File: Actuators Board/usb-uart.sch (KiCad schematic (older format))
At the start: 15 parts

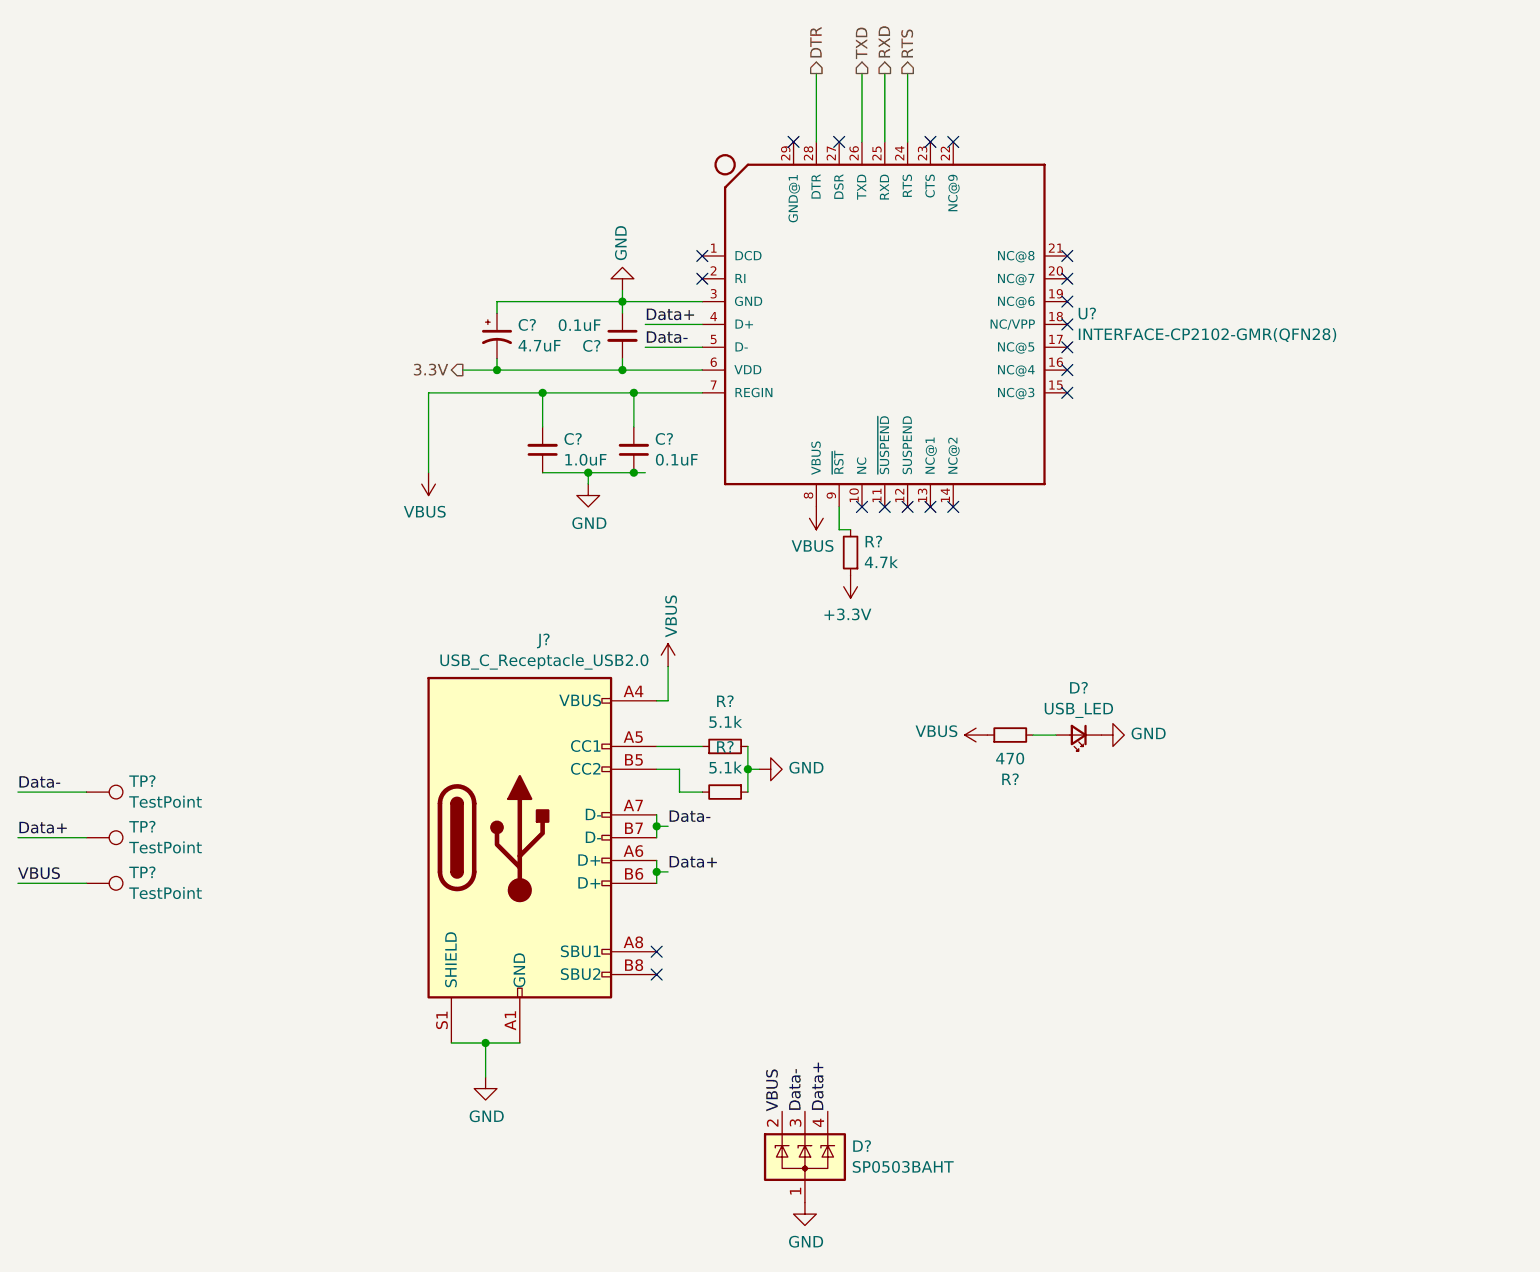
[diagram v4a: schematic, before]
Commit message: Most footprint assignments on dc motor board
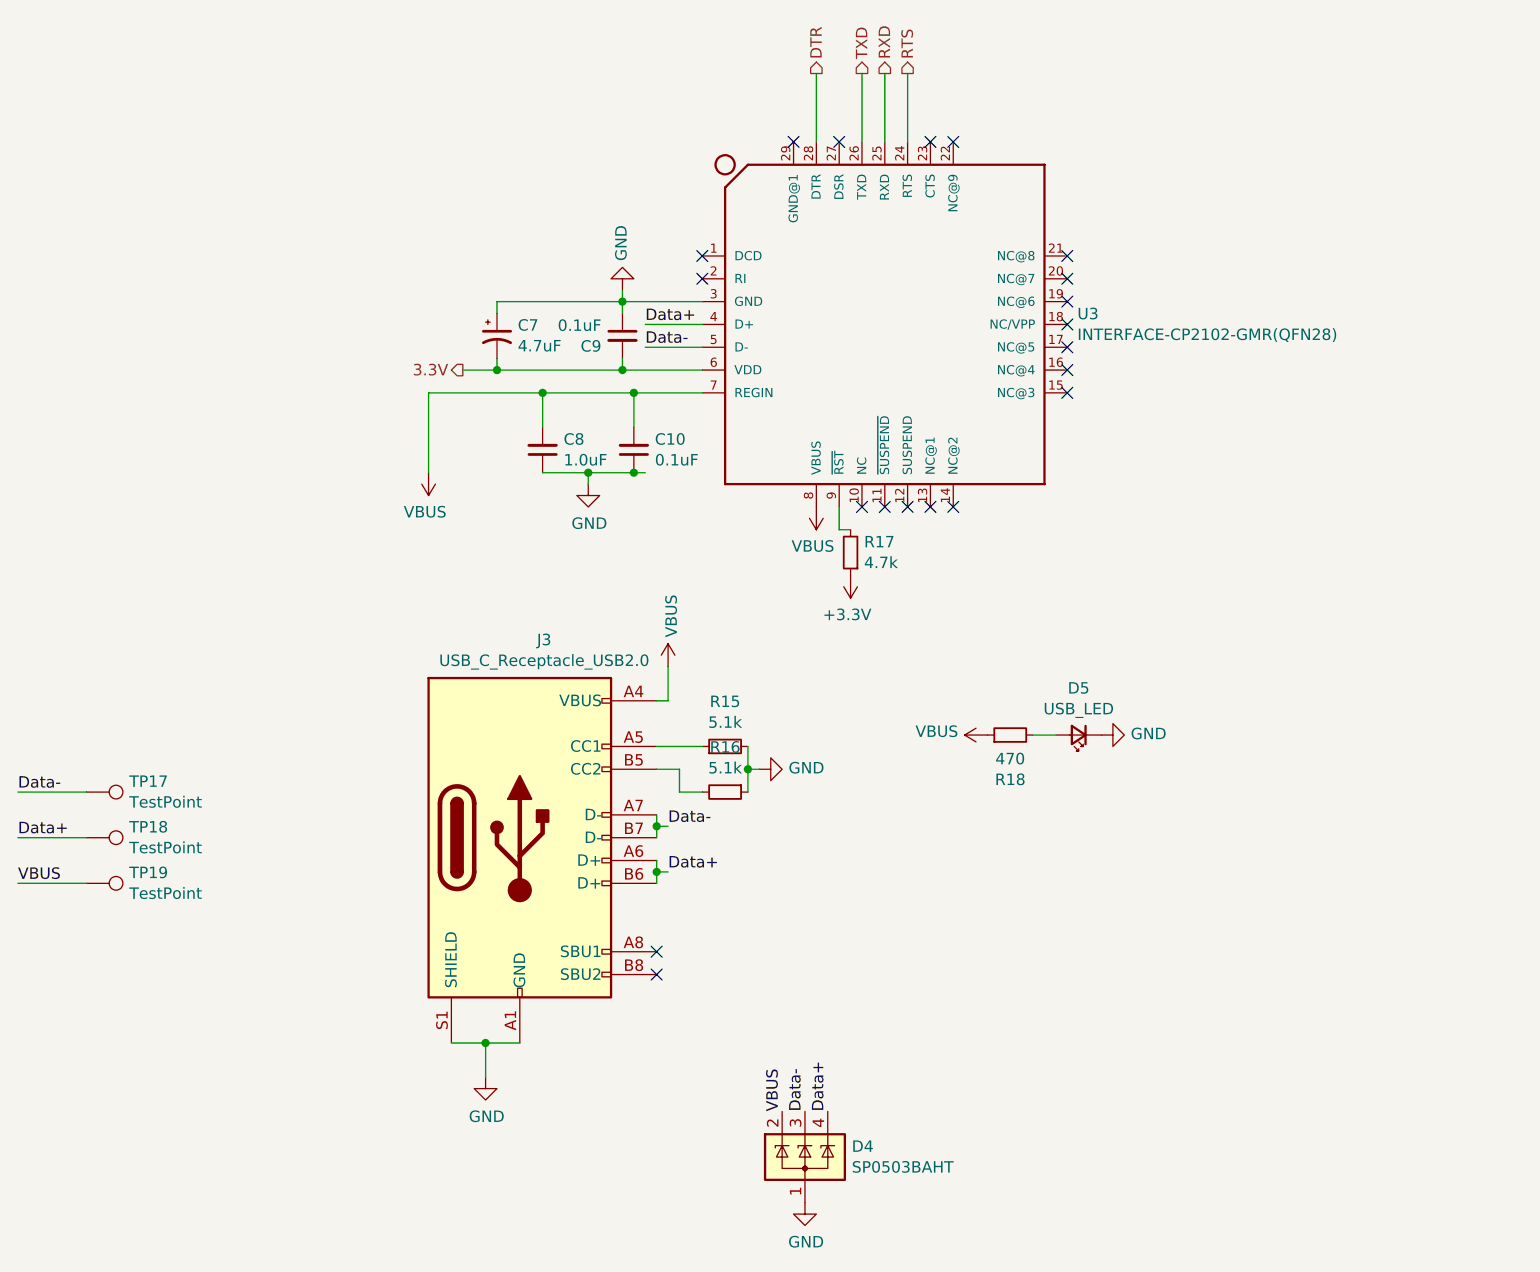
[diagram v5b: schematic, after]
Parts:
- C10, C7, C8, C9: renamed from C?; footprint (none) -> Capacitor_SMD:C_0603_1608Metric
- R15, R16, R17: renamed from R?; footprint (none) -> Resistor_SMD:R_0603_1608Metric
- TP17, TP18, TP19: renamed from TP?; footprint (none) -> TestPoint:TestPoint_THTPad_1.0x1.0mm_Drill0.5mm
- U3: renamed from U?; footprint QFN28G_0.5-5X5MM -> iclr:QFN28G_0.5-5X5MM
- gave numbers to parts that had none: 4
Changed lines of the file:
@@
 P 5000 3800
 AR Path="/61988BF8" Ref="#PWR?"  Part="1"
-AR Path="/61925999/61988BF8" Ref="#PWR?"  Part="1"
+AR Path="/61925999/61988BF8" Ref="#PWR0119"  Part="1"
 AR Path="/61997866/61988BF8" Ref="#PWR?"  Part="1"
-F 0 "#PWR?" H 5000 3550 50  0001 C CNN
+F 0 "#PWR0119" H 5000 3550 50  0001 C CNN
 F 1 "GND" V 5005 3672 50  0000 R CNN
 F 2 "" H 5000 3800 50  0001 C CNN
@@
 P 4850 3900
 AR Path="/61988C01" Ref="R?"  Part="1"
-AR Path="/61925999/61988C01" Ref="R?"  Part="1"
+AR Path="/61925999/61988C01" Ref="R16"  Part="1"
 AR Path="/61997866/61988C01" Ref="R?"  Part="1"
-F 0 "R?" V 4654 3900 50  0000 C CNN
+F 0 "R16" V 4654 3900 50  0000 C CNN
 F 1 "5.1k" V 4745 3900 50  0000 C CNN
-F 2 "" H 4850 3900 50  0001 C CNN
+F 2 "Resistor_SMD:R_0603_1608Metric" H 4850 3900 50  0001 C CNN
 F 3 "~" H 4850 3900 50  0001 C CNN
 	1    4850 3900
@@
 P 4850 3700
 AR Path="/61988C0E" Ref="R?"  Part="1"
-AR Path="/61925999/61988C0E" Ref="R?"  Part="1"
+AR Path="/61925999/61988C0E" Ref="R15"  Part="1"
 AR Path="/61997866/61988C0E" Ref="R?"  Part="1"
-F 0 "R?" V 5046 3700 50  0000 C CNN
+F 0 "R15" V 5046 3700 50  0000 C CNN
 F 1 "5.1k" V 4955 3700 50  0000 C CNN
-F 2 "" H 4850 3700 50  0001 C CNN
+F 2 "Resistor_SMD:R_0603_1608Metric" H 4850 3700 50  0001 C CNN
 F 3 "~" H 4850 3700 50  0001 C CNN
 	1    4850 3700
@@
 P 3800 5150
 AR Path="/61988C18" Ref="#PWR?"  Part="1"
-AR Path="/61925999/61988C18" Ref="#PWR?"  Part="1"
+AR Path="/61925999/61988C18" Ref="#PWR0120"  Part="1"
 AR Path="/61997866/61988C18" Ref="#PWR?"  Part="1"
-F 0 "#PWR?" H 3800 4900 50  0001 C CNN
+F 0 "#PWR0120" H 3800 4900 50  0001 C CNN
 F 1 "GND" H 3805 4977 50  0000 C CNN
 F 2 "" H 3800 5150 50  0001 C CNN
@@
 P 3950 4100
 AR Path="/61988C49" Ref="J?"  Part="1"
-AR Path="/61925999/61988C49" Ref="J?"  Part="1"
+AR Path="/61925999/61988C49" Ref="J3"  Part="1"
 AR Path="/61997866/61988C49" Ref="J?"  Part="1"
-F 0 "J?" H 4057 4967 50  0000 C CNN
+F 0 "J3" H 4057 4967 50  0000 C CNN
 F 1 "USB_C_Receptacle_USB2.0" H 4057 4876 50  0000 C CNN
 F 2 "" H 4100 4100 50  0001 C CNN
@@
 P 5200 5700
 AR Path="/61988C86" Ref="#PWR?"  Part="1"
-AR Path="/61925999/61988C86" Ref="#PWR?"  Part="1"
+AR Path="/61925999/61988C86" Ref="#PWR0121"  Part="1"
 AR Path="/61997866/61988C86" Ref="#PWR?"  Part="1"
-F 0 "#PWR?" H 5200 5450 50  0001 C CNN
+F 0 "#PWR0121" H 5200 5450 50  0001 C CNN
 F 1 "GND" H 5205 5527 50  0000 C CNN
 F 2 "" H 5200 5700 50  0001 C CNN
@@
 P 5200 5500
 AR Path="/61988C8C" Ref="D?"  Part="1"
-AR Path="/61925999/61988C8C" Ref="D?"  Part="1"
+AR Path="/61925999/61988C8C" Ref="D4"  Part="1"
 AR Path="/61997866/61988C8C" Ref="D?"  Part="1"
-F 0 "D?" H 5405 5546 50  0000 L CNN
+F 0 "D4" H 5405 5546 50  0000 L CNN
 F 1 "SP0503BAHT" H 5405 5455 50  0000 L CNN
 F 2 "Package_TO_SOT_SMD:SOT-143" H 5425 5450 50  0001 L CNN
@@
 	4550 4250 4550 4300
 $Comp
-L power:GND #PWR?
+L power:GND #PWR0122
 U 1 1 619952DA
 P 4400 1700
-F 0 "#PWR?" H 4400 1450 50  0001 C CNN
+F 0 "#PWR0122" H 4400 1450 50  0001 C CNN
 F 1 "GND" V 4405 1572 50  0000 R CNN
 F 2 "" H 4400 1700 50  0001 C CNN
@@
 $EndComp
 $Comp
-L power:VBUS #PWR?
+L power:VBUS #PWR0123
 U 1 1 61996CDA
 P 5250 2650
-F 0 "#PWR?" H 5250 2500 50  0001 C CNN
+F 0 "#PWR0123" H 5250 2500 50  0001 C CNN
 F 1 "VBUS" H 5265 2823 50  0000 C CNN
 F 2 "" H 5250 2650 50  0001 C CNN
@@
 NoConn ~ 5650 2650
 $Comp
-L power:VBUS #PWR?
+L power:VBUS #PWR0124
 U 1 1 61A236C4
 P 4600 3350
-F 0 "#PWR?" H 4600 3200 50  0001 C CNN
+F 0 "#PWR0124" H 4600 3200 50  0001 C CNN
 F 1 "VBUS" V 4615 3478 50  0000 L CNN
 F 2 "" H 4600 3350 50  0001 C CNN
@@
 	4400 1700 4400 1750
 $Comp
-L Device:C_Small C?
+L Device:C_Small C10
 U 1 1 61A2A124
 P 4450 2400
-F 0 "C?" H 4358 2354 50  0000 R CNN
+F 0 "C10" H 4358 2354 50  0000 R CNN
 F 1 "0.1uF" H 4358 2445 50  0000 R CNN
-F 2 "" H 4450 2400 50  0001 C CNN
+F 2 "Capacitor_SMD:C_0603_1608Metric" H 4450 2400 50  0001 C CNN
 F 3 "~" H 4450 2400 50  0001 C CNN
 	1    4450 2400
@@
 $EndComp
 $Comp
-L Device:C_Small C?
+L Device:C_Small C8
 U 1 1 61A28787
 P 4050 2400
-F 0 "C?" H 3958 2354 50  0000 R CNN
+F 0 "C8" H 3958 2354 50  0000 R CNN
 F 1 "1.0uF" H 3958 2445 50  0000 R CNN
-F 2 "" H 4050 2400 50  0001 C CNN
+F 2 "Capacitor_SMD:C_0603_1608Metric" H 4050 2400 50  0001 C CNN
 F 3 "~" H 4050 2400 50  0001 C CNN
 	1    4050 2400
@@
 	4050 2500 4250 2500
 $Comp
-L power:GND #PWR?
+L power:GND #PWR0125
 U 1 1 61A3A0E4
 P 4250 2550
-F 0 "#PWR?" H 4250 2300 50  0001 C CNN
+F 0 "#PWR0125" H 4250 2300 50  0001 C CNN
 F 1 "GND" H 4255 2377 50  0000 C CNN
 F 2 "" H 4250 2550 50  0001 C CNN
@@
 Connection ~ 4450 2150
 $Comp
-L power:VBUS #PWR?
+L power:VBUS #PWR0126
 U 1 1 61A46D5F
 P 3550 2500
-F 0 "#PWR?" H 3550 2350 50  0001 C CNN
+F 0 "#PWR0126" H 3550 2350 50  0001 C CNN
 F 1 "VBUS" H 3565 2673 50  0000 C CNN
 F 2 "" H 3550 2500 50  0001 C CNN
@@
 NoConn ~ 5150 1050
 $Comp
-L Device:R_Small R?
+L Device:R_Small R17
 U 1 1 61A58884
 P 5400 2850
-F 0 "R?" H 5341 2804 50  0000 R CNN
+F 0 "R17" H 5341 2804 50  0000 R CNN
 F 1 "4.7k" H 5341 2895 50  0000 R CNN
-F 2 "" H 5400 2850 50  0001 C CNN
+F 2 "Resistor_SMD:R_0603_1608Metric" H 5400 2850 50  0001 C CNN
 F 3 "~" H 5400 2850 50  0001 C CNN
 	1    5400 2850
@@
 	4450 2150 4750 2150
 $Comp
-L iclr:INTERFACE-CP2102-GMR(QFN28) U?
+L iclr:INTERFACE-CP2102-GMR(QFN28) U3
 U 1 1 6198EFBF
 P 5550 1850
-F 0 "U?" H 6394 1896 50  0000 L CNN
+F 0 "U3" H 6394 1896 50  0000 L CNN
 F 1 "INTERFACE-CP2102-GMR(QFN28)" H 6394 1805 50  0000 L CNN
-F 2 "QFN28G_0.5-5X5MM" H 5550 1850 50  0001 L BNN
+F 2 "iclr:QFN28G_0.5-5X5MM" H 5550 1850 50  0001 L BNN
 F 3 "" H 5550 1850 50  0001 L BNN
 F 4 "CP2102-GMR-QFN28" H 5550 1850 50  0001 L BNN "VALUE"
@@
 P 5400 2950
 AR Path="/61A9124D" Ref="#PWR?"  Part="1"
-AR Path="/61925999/61A9124D" Ref="#PWR?"  Part="1"
+AR Path="/61925999/61A9124D" Ref="#PWR0127"  Part="1"
 AR Path="/61997866/61A9124D" Ref="#PWR?"  Part="1"
-F 0 "#PWR?" H 5400 2800 50  0001 C CNN
+F 0 "#PWR0127" H 5400 2800 50  0001 C CNN
 F 1 "+3.3V" H 5415 3123 50  0000 C CNN
 F 2 "" H 5400 2950 50  0001 C CNN
@@
 3.3V
 $Comp
-L Device:C_Small C?
+L Device:C_Small C9
 U 1 1 61AA33A7
 P 4400 1900
-F 0 "C?" H 4308 1854 50  0000 R CNN
+F 0 "C9" H 4308 1854 50  0000 R CNN
 F 1 "0.1uF" H 4308 1945 50  0000 R CNN
-F 2 "" H 4400 1900 50  0001 C CNN
+F 2 "Capacitor_SMD:C_0603_1608Metric" H 4400 1900 50  0001 C CNN
 F 3 "~" H 4400 1900 50  0001 C CNN
 	1    4400 1900
@@
 $EndComp
 $Comp
-L Device:CP1_Small C?
+L Device:CP1_Small C7
 U 1 1 61AA4224
 P 3850 1900
-F 0 "C?" H 3941 1946 50  0000 L CNN
+F 0 "C7" H 3941 1946 50  0000 L CNN
 F 1 "4.7uF" H 3941 1855 50  0000 L CNN
-F 2 "" H 3850 1900 50  0001 C CNN
+F 2 "Capacitor_SMD:C_0603_1608Metric" H 3850 1900 50  0001 C CNN
 F 3 "~" H 3850 1900 50  0001 C CNN
 	1    3850 1900
@@
 	3850 1750 4400 1750
 $Comp
-L Connector:TestPoint TP?
+L Connector:TestPoint TP17
 U 1 1 61AB7CB8
 P 2050 3900
-F 0 "TP?" V 2004 4088 50  0000 L CNN
+F 0 "TP17" V 2004 4088 50  0000 L CNN
 F 1 "TestPoint" V 2095 4088 50  0000 L CNN
-F 2 "" H 2250 3900 50  0001 C CNN
+F 2 "TestPoint:TestPoint_THTPad_1.0x1.0mm_Drill0.5mm" H 2250 3900 50  0001 C CNN
 F 3 "~" H 2250 3900 50  0001 C CNN
 	1    2050 3900
@@
 $EndComp
 $Comp
-L Connector:TestPoint TP?
+L Connector:TestPoint TP18
 U 1 1 61AB87F3
 P 2050 4100
-F 0 "TP?" V 2004 4288 50  0000 L CNN
+F 0 "TP18" V 2004 4288 50  0000 L CNN
 F 1 "TestPoint" V 2095 4288 50  0000 L CNN
-F 2 "" H 2250 4100 50  0001 C CNN
+F 2 "TestPoint:TestPoint_THTPad_1.0x1.0mm_Drill0.5mm" H 2250 4100 50  0001 C CNN
 F 3 "~" H 2250 4100 50  0001 C CNN
 	1    2050 4100
@@
 $EndComp
 $Comp
-L Connector:TestPoint TP?
+L Connector:TestPoint TP19
 U 1 1 61AB9568
 P 2050 4300
-F 0 "TP?" V 2004 4488 50  0000 L CNN
+F 0 "TP19" V 2004 4488 50  0000 L CNN
 F 1 "TestPoint" V 2095 4488 50  0000 L CNN
-F 2 "" H 2250 4300 50  0001 C CNN
+F 2 "TestPoint:TestPoint_THTPad_1.0x1.0mm_Drill0.5mm" H 2250 4300 50  0001 C CNN
 F 3 "~" H 2250 4300 50  0001 C CNN
 	1    2050 4300
@@
 P 6400 3650
 AR Path="/61B104EA" Ref="D?"  Part="1"
-AR Path="/61925999/61B104EA" Ref="D?"  Part="1"
-F 0 "D?" H 6400 3445 50  0000 C CNN
+AR Path="/61925999/61B104EA" Ref="D5"  Part="1"
+F 0 "D5" H 6400 3445 50  0000 C CNN
 F 1 "USB_LED" H 6400 3536 50  0000 C CNN
 F 2 "LED_SMD:LED_0603_1608Metric_Castellated" V 6400 3650 50  0001 C CNN
@@
 $EndComp
 $Comp
-L Device:R_Small R?
+L Device:R_Small R18
 U 1 1 61B104F0
 P 6100 3650
-F 0 "R?" V 5904 3650 50  0000 C CNN
+F 0 "R18" V 5904 3650 50  0000 C CNN
 F 1 "470" V 5995 3650 50  0000 C CNN
 F 2 "Resistor_SMD:R_0603_1608Metric" H 6100 3650 50  0001 C CNN
@@
 P 6500 3650
 AR Path="/61B11F2F" Ref="#PWR?"  Part="1"
-AR Path="/61925999/61B11F2F" Ref="#PWR?"  Part="1"
+AR Path="/61925999/61B11F2F" Ref="#PWR0128"  Part="1"
 AR Path="/61997866/61B11F2F" Ref="#PWR?"  Part="1"
-F 0 "#PWR?" H 6500 3400 50  0001 C CNN
+F 0 "#PWR0128" H 6500 3400 50  0001 C CNN
 F 1 "GND" V 6505 3522 50  0000 R CNN
 F 2 "" H 6500 3650 50  0001 C CNN
@@
 $EndComp
 $Comp
-L power:VBUS #PWR?
+L power:VBUS #PWR0129
 U 1 1 61B168A6
 P 6000 3650
-F 0 "#PWR?" H 6000 3500 50  0001 C CNN
+F 0 "#PWR0129" H 6000 3500 50  0001 C CNN
 F 1 "VBUS" V 6015 3778 50  0000 L CNN
 F 2 "" H 6000 3650 50  0001 C CNN

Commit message: More footprint assignments, imported components into PCB
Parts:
- J3: footprint (none) -> Connector_USB:USB_C_Receptacle_GCT_USB4085
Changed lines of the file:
@@
 F 0 "J3" H 4057 4967 50  0000 C CNN
 F 1 "USB_C_Receptacle_USB2.0" H 4057 4876 50  0000 C CNN
-F 2 "" H 4100 4100 50  0001 C CNN
+F 2 "Connector_USB:USB_C_Receptacle_GCT_USB4085" H 4100 4100 50  0001 C CNN
 F 3 "https://www.usb.org/sites/default/files/documents/usb_type-c.zip" H 4100 4100 50  0001 C CNN
 	1    3950 4100

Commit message: Updated footprint for C7, grouped USB components together
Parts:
- C7: footprint Capacitor_SMD:C_0603_1608Metric -> Capacitor_SMD:CP_Elec_3x5.3
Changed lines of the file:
@@
 F 0 "C7" H 3941 1946 50  0000 L CNN
 F 1 "4.7uF" H 3941 1855 50  0000 L CNN
-F 2 "Capacitor_SMD:C_0603_1608Metric" H 3850 1900 50  0001 C CNN
+F 2 "Capacitor_SMD:CP_Elec_3x5.3" H 3850 1900 50  0001 C CNN
 F 3 "~" H 3850 1900 50  0001 C CNN
 	1    3850 1900

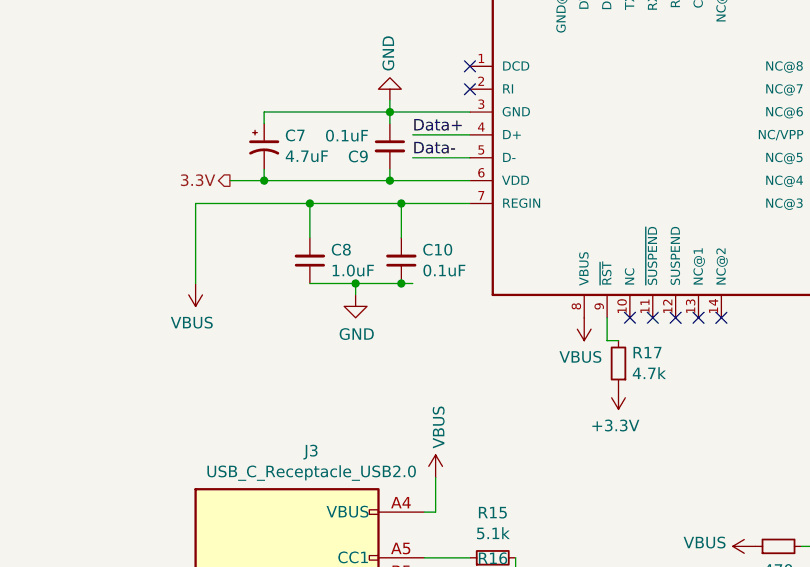
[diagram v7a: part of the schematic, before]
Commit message: Combined the 3 boards into one
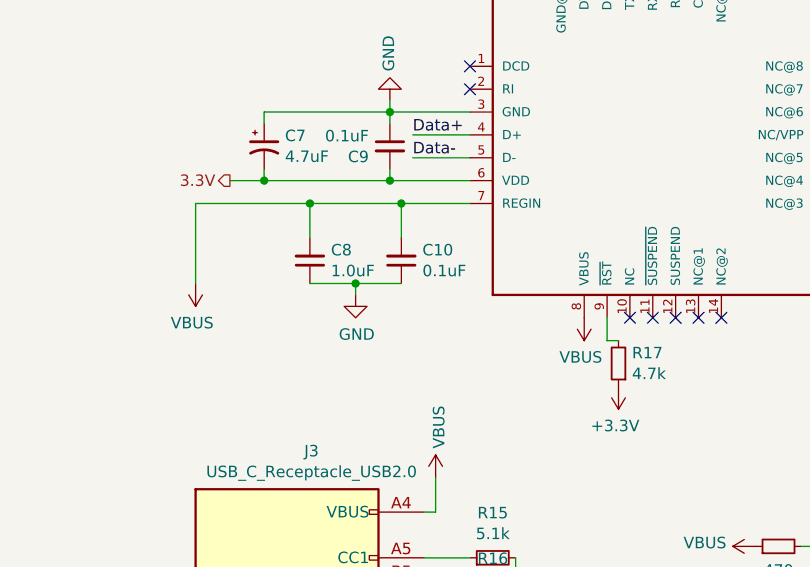
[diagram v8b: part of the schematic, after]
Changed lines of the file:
@@
 	4400 1700 4400 1750
-$Comp
-L Device:C_Small C10
-U 1 1 61A2A124
-P 4450 2400
-F 0 "C10" H 4358 2354 50  0000 R CNN
-F 1 "0.1uF" H 4358 2445 50  0000 R CNN
-F 2 "Capacitor_SMD:C_0603_1608Metric" H 4450 2400 50  0001 C CNN
-F 3 "~" H 4450 2400 50  0001 C CNN
-	1    4450 2400
-	-1   0    0    1
-$EndComp
 $Comp
 L Device:C_Small C8
@@
 Wire Wire Line
 	4050 2150 4450 2150
-Wire Wire Line
-	4450 2500 4500 2500
-Connection ~ 4450 2500
 Connection ~ 4450 2150
 $Comp
@@
 	0    -1   -1   0
 $EndComp
+$Comp
+L Device:C_Small C10
+U 1 1 61A2A124
+P 4450 2400
+F 0 "C10" H 4358 2354 50  0000 R CNN
+F 1 "0.1uF" H 4358 2445 50  0000 R CNN
+F 2 "Capacitor_SMD:C_0603_1608Metric" H 4450 2400 50  0001 C CNN
+F 3 "~" H 4450 2400 50  0001 C CNN
+	1    4450 2400
+	-1   0    0    1
+$EndComp
 $EndSCHEMATC
